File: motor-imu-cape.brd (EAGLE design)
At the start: 54.3 x 58.4 mm, 20 parts, among them IC1 40109, IC2 40109, IC3 24LC256P

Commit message: Board WIP
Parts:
- moved JP2 89.2 mm to (36.8, 30.5)
- moved SV10 85.4 mm to (24.1, 2.54)
- moved SV13 80.2 mm to (12.7, 2.54)
- moved IC1 78.5 mm to (27.9, 44.5), turned to 270 degrees
- moved R2 76.4 mm to (14.0, 39.4)
- moved SV9 73.6 mm to (24.1, 8.89)
- moved SV7 73.4 mm to (33.0, 11.4), turned to 270 degrees
- moved IC2 69.5 mm to (41.9, 44.5), turned to 270 degrees
- moved R1 65.6 mm to (14.0, 43.2)
- moved SV12 65.6 mm to (12.7, 8.89)
- moved R5 64.5 mm to (14.0, 27.9)
- moved C1 63.2 mm to (14.0, 24.1)
- moved SV8 62.0 mm to (24.1, 15.2)
- moved IC3 57.9 mm to (14.0, 52.1), turned to 270 degrees
- moved R4 54.2 mm to (14.0, 31.8)
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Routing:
- added copper zone on layer 16, net GND

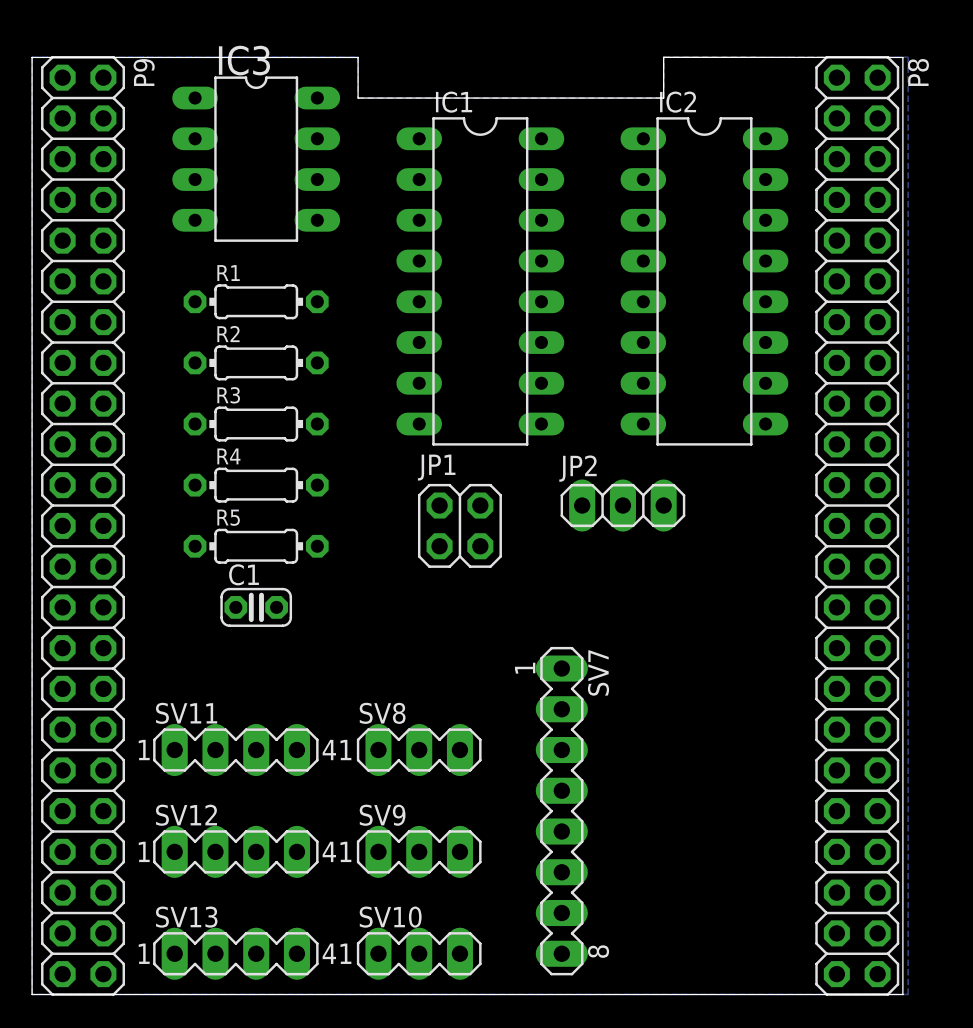
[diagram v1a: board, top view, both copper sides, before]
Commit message: Fix issues with ground planes.
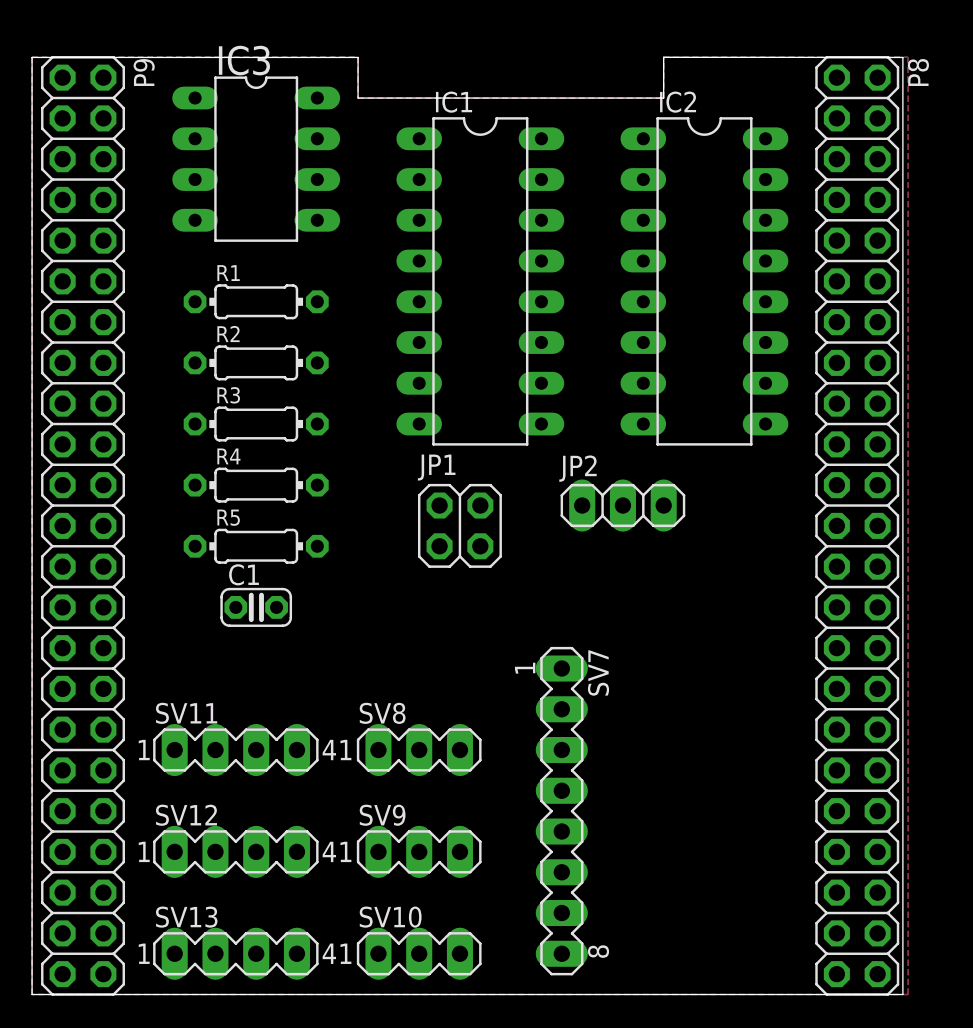
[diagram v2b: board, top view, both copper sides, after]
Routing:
- added copper zone on layer 1, net GND
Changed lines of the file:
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@@
 <contactref element="JP1" pad="3"/>
 <contactref element="IC3" pad="7"/>
-<polygon width="0.4064" layer="16" isolate="4.064">
+<polygon width="0.4064" layer="16" isolate="0.254" orphans="yes">
 <vertex x="0" y="58.42"/>
 <vertex x="20.32" y="58.42"/>
@@
 <vertex x="0" y="0"/>
 </polygon>
-<wire x1="27.94" y1="27.94" x2="38.1" y2="35.56" width="0" layer="19" extent="1-1"/>
-<wire x1="25.4" y1="27.94" x2="27.94" y2="27.94" width="0" layer="19" extent="1-1"/>
-<wire x1="24.13" y1="35.56" x2="25.4" y2="27.94" width="0" layer="19" extent="1-1"/>
-<wire x1="15.24" y1="24.13" x2="25.4" y2="27.94" width="0" layer="19" extent="1-1"/>
-<wire x1="13.97" y1="15.24" x2="15.24" y2="24.13" width="0" layer="19" extent="1-1"/>
-<wire x1="13.97" y1="8.89" x2="13.97" y2="15.24" width="0" layer="19" extent="1-1"/>
-<wire x1="13.97" y1="2.54" x2="13.97" y2="8.89" width="0" layer="19" extent="1-1"/>
-<wire x1="21.59" y1="15.24" x2="13.97" y2="15.24" width="0" layer="19" extent="1-1"/>
-<wire x1="21.59" y1="8.89" x2="21.59" y2="15.24" width="0" layer="19" extent="1-1"/>
-<wire x1="21.59" y1="2.54" x2="21.59" y2="8.89" width="0" layer="19" extent="1-1"/>
-<wire x1="4.445" y1="3.81" x2="13.97" y2="2.54" width="0" layer="19" extent="1-1"/>
-<wire x1="1.905" y1="3.81" x2="4.445" y2="3.81" width="0" layer="19" extent="1-1"/>
-<wire x1="4.445" y1="1.27" x2="4.445" y2="3.81" width="0" layer="19" extent="1-1"/>
-<wire x1="1.905" y1="1.27" x2="1.905" y2="3.81" width="0" layer="19" extent="1-1"/>
-<wire x1="33.02" y1="17.78" x2="27.94" y2="27.94" width="0" layer="19" extent="1-1"/>
-<wire x1="17.78" y1="53.34" x2="24.13" y2="35.56" width="0" layer="19" extent="1-1"/>
-<wire x1="10.16" y1="48.26" x2="17.78" y2="53.34" width="0" layer="19" extent="1-1"/>
+<polygon width="0.4064" layer="1" isolate="0.254" orphans="yes">
+<vertex x="0" y="58.42"/>
+<vertex x="20.32" y="58.42"/>
+<vertex x="20.32" y="55.88"/>
+<vertex x="39.37" y="55.88"/>
+<vertex x="39.37" y="58.42"/>
+<vertex x="54.61" y="58.42"/>
+<vertex x="54.61" y="0"/>
+<vertex x="0" y="0"/>
+</polygon>
 </signal>
 <signal name="QEP1A">
